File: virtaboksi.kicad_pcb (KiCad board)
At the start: 2 copper layers, 50 x 71.9 mm, 61 parts, among them J1 Panel_01x08, J2 Ext_01x05, J3 Powerpole 01x02, J4 Powerpole 01x02, J5 Powerpole 01x02, J6 Conn_01x03_Male, J7 TagConnect_TC2030-NL, Q1 2N7002, Q2 IRF4905, Q3 IRF4905, Q4 2N7002, Q5 IRF4905, Q6 IRF4905, Q7 2N7002, Q8 IRF4905, Q9 IRF4905, U1 SRV05-4, U2 AMSRI-783.3-NZ, U3 STM8S003F3P, U4 SRV05-4, U5 SP3485EN

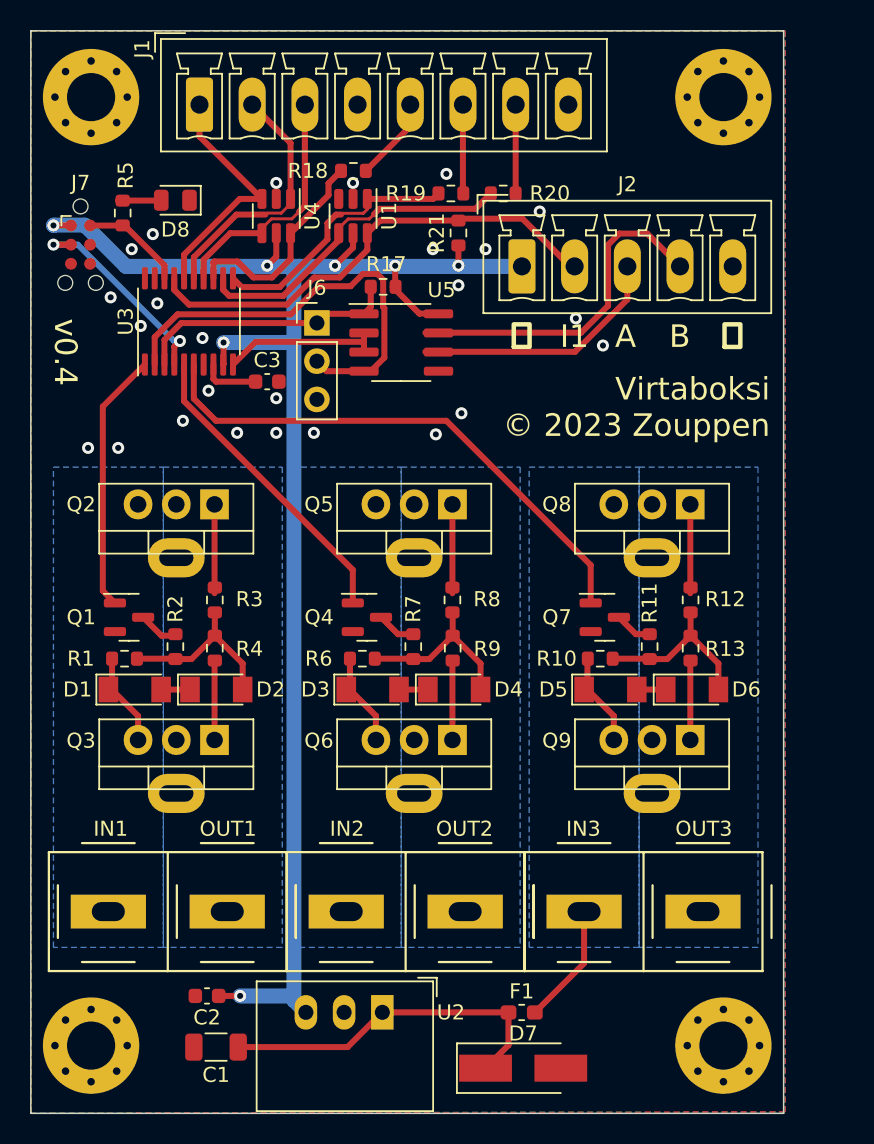
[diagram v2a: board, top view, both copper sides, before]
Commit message: Update solder mask, do final tweaks, make it pass ERC & DRC
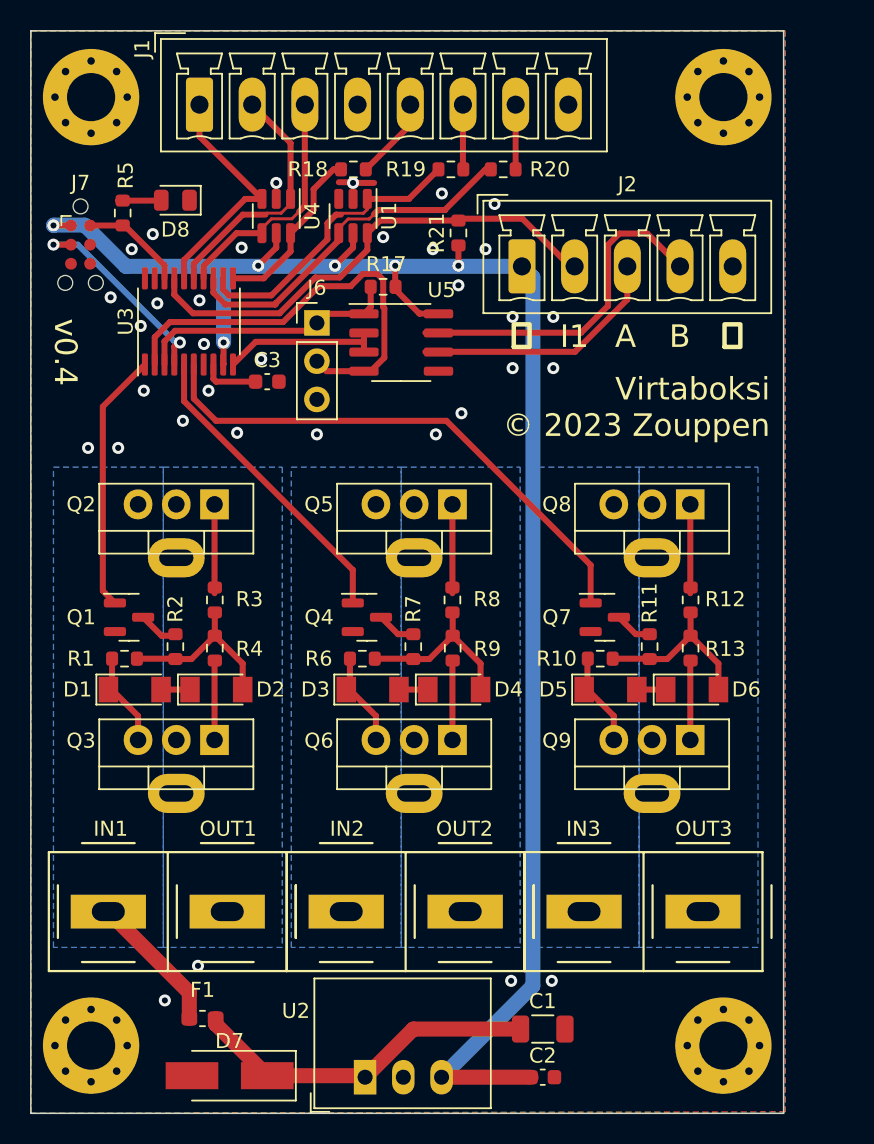
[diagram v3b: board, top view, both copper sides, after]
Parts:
- J6: value Conn_01x03_Male -> Optional_01x03
- moved C2 22.9 mm to (141.5, 109.5), turned to 0 degrees
- moved C1 21.7 mm to (141.5, 106.3), turned to 0 degrees
- moved F1 21.2 mm to (118.9, 105.6), turned to 0 degrees
- moved D7 19.5 mm to (120.7, 109.4), turned to 180 degrees
- moved U2 4.46 mm to (129.7, 109.5), turned to 0 degrees
- moved R19 1.60 mm to (135.4, 49.2)
- moved R20 1.60 mm to (138.9, 49.2)
- moved R18 0.10 mm to (128.9, 49.2)
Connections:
- F1 pad 1: /GROUP3 IN -> /GROUP1 IN
- U3 pad 11: /LED2 -> /LED1
- U3 pad 12: /LED3 -> /LED2
- U3 pad 13: /LED1 -> /LED3
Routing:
- net /GROUP1 IN: track 5.99 -> 15.3 mm
- net +3.3V: track 106.0 -> 114.8 mm, vias 7 -> 6
- net /GROUP3 IN: track 14.0 -> 5.99 mm
- net /LED1: track 14.4 -> 11.7 mm
- net GND: track 0.00 -> 2.36 mm, vias 25 -> 34
- net /LED2: track 17.5 -> 19.7 mm
- net /LED3: track 22.4 -> 24.3 mm
- net Net-(J1-Pad6): track 5.91 -> 4.31 mm
- net Net-(J1-Pad7): track 5.90 -> 4.30 mm
- net /IN1: track 31.3 -> 32.0 mm

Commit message: Reannotate everything
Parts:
- renumbered D7 to D1, D8 to D2, D1 to D3, D2 to D4, D3 to D5, D4 to D6, D5 to D7, D6 to D8, J6 to J1, J1 to J3, J3 to J4, J4 to J5, J5 to J6, R21 to R1, R4 to R10, R6 to R11, R7 to R12, R8 to R13, R9 to R14, R10 to R15, R11 to R16, R12 to R17, R13 to R18, R18 to R2, R19 to R3, R20 to R4, R17 to R5, R5 to R6, R1 to R7, R2 to R8, R3 to R9, U4 to U1, U1 to U3, U5 to U4, U3 to U5

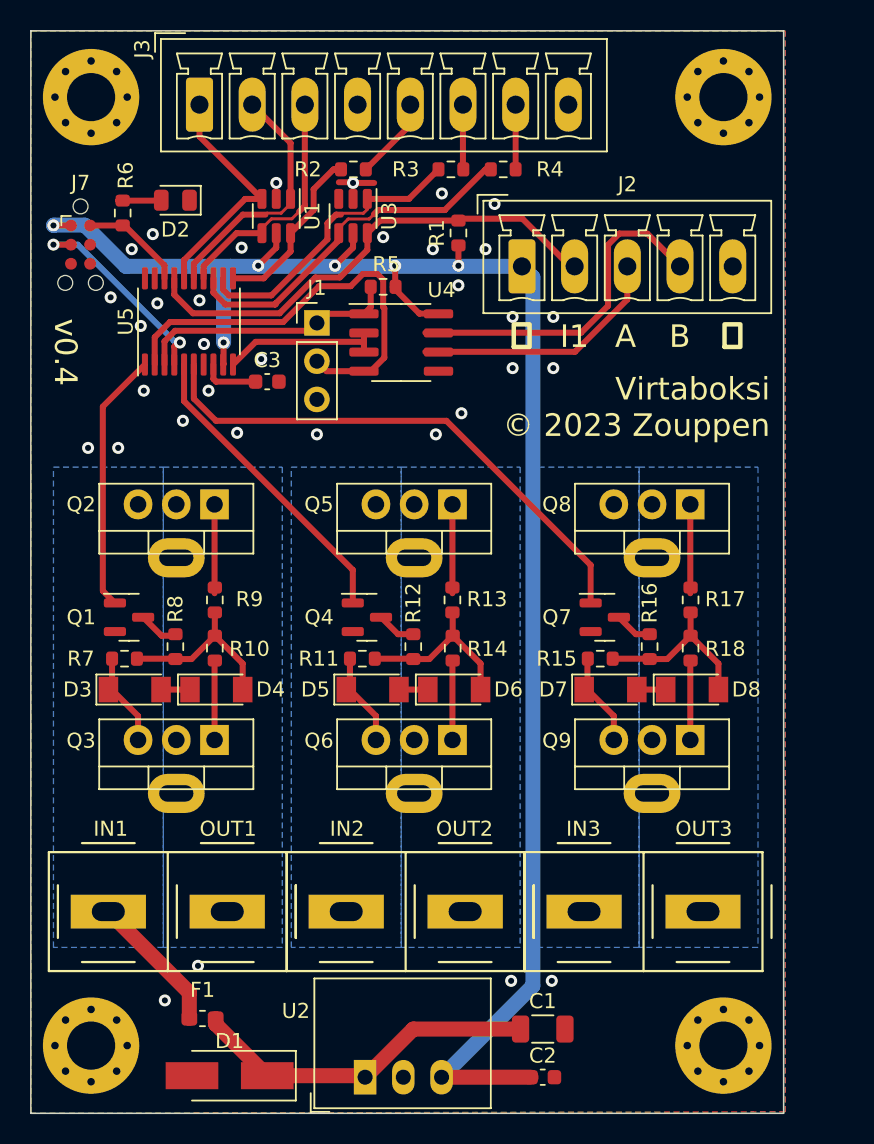
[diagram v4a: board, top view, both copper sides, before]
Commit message: Throw fuse out of the window, clear space left of J2, add 2 extra pins
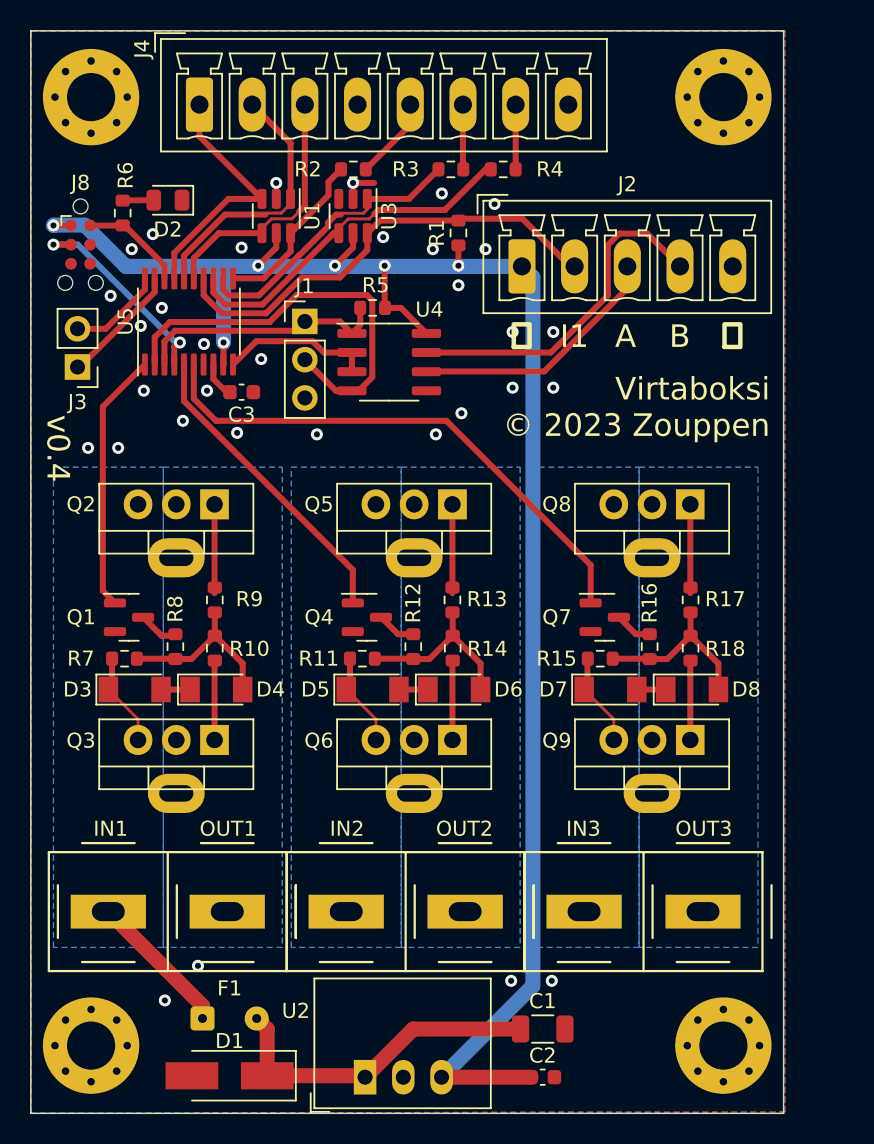
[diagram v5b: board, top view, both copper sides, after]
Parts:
- added J3: Optional_01x02_Male, Connector_PinHeader_2.54mm:PinHeader_1x02_P2.54mm_Vertical, F.Cu at (110.6, 62.3)
- F1: footprint Fuse:Fuse_0603_1608Metric_Pad1.05x0.95mm_HandSolder -> Connector_Wire:SolderWire-0.1sqmm_1x02_P3.6mm_D0.4mm_OD1mm
- moved C3 1.84 mm to (121.5, 64.0)
- moved R5 1.57 mm to (130.2, 58.4)
- moved U4 1.53 mm to (131.3, 62.0)
- moved J1 0.81 mm to (125.7, 59.3)
- moved D2 0.50 mm to (116.6, 51.2)
- renumbered J3 to J4, J4 to J5, J5 to J6, J6 to J7, J7 to J8
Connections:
- U5 pad 14: /IN4 -> /IN1
- U5 pad 15: /IN3 -> /IN4
- U5 pad 16: /IN2 -> /IN3
- U5 pad 17: /IN1 -> /IN2
- U5 pad 19: unconnected-(U5-Pad19) -> /EXTRA1
- U5 pad 20: unconnected-(U5-Pad20) -> /EXTRA2
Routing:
- net /EXTRA1: track 0.00 -> 8.10 mm
- net /EXTRA2: track 0.00 -> 6.30 mm
- net +3.3V: track 114.8 -> 116.7 mm
- net /IN1: track 32.0 -> 30.1 mm
- net Net-(C3-Pad1): track 3.83 -> 2.42 mm
- net Net-(C1-Pad1): track 23.4 -> 22.3 mm
- net GND: track 2.36 -> 1.40 mm, vias 34 -> 33
- net /IN3: track 16.7 -> 17.7 mm
- net /IN4: track 16.1 -> 17.1 mm
- net /IN2: track 16.1 -> 17.0 mm
- net /TX: track 29.2 -> 28.4 mm
- net /RX: track 17.5 -> 16.8 mm
- net Net-(D2-Pad2): track 2.66 -> 2.07 mm

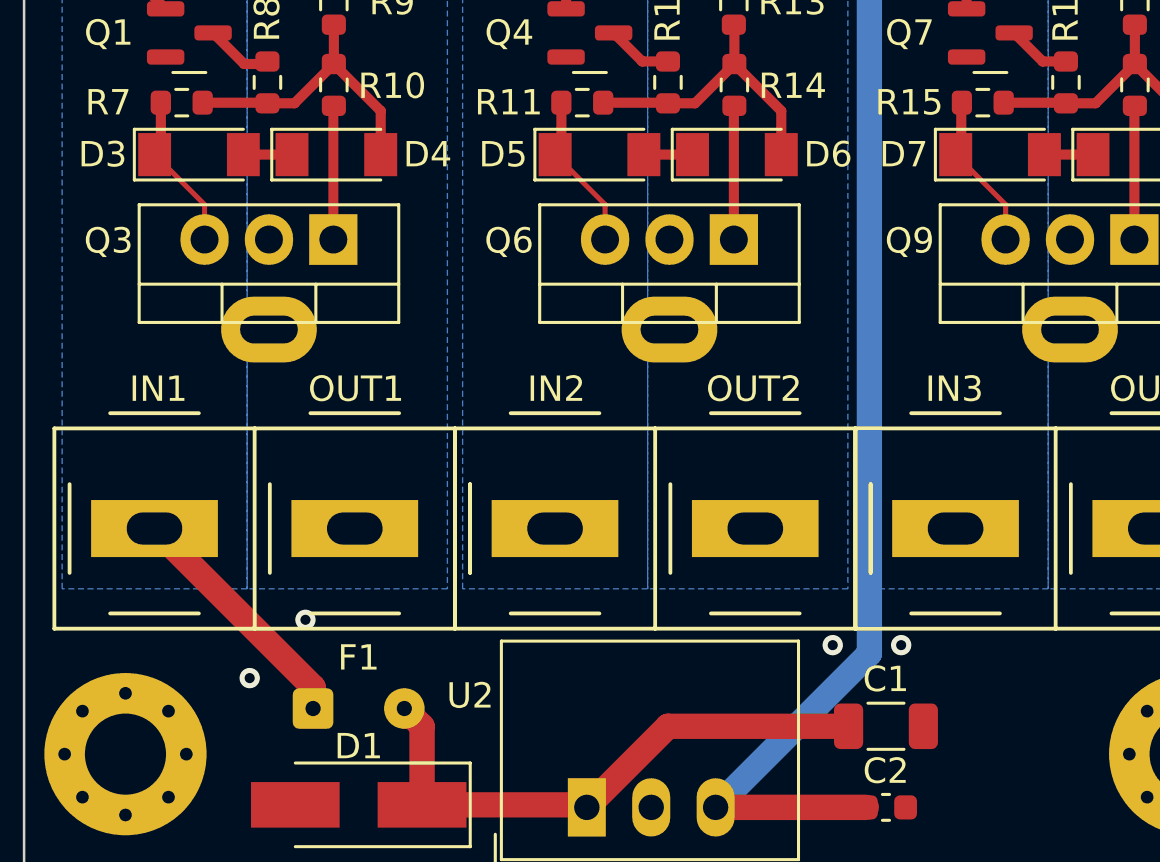
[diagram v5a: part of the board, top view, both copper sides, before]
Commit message: Add makeshift fuse
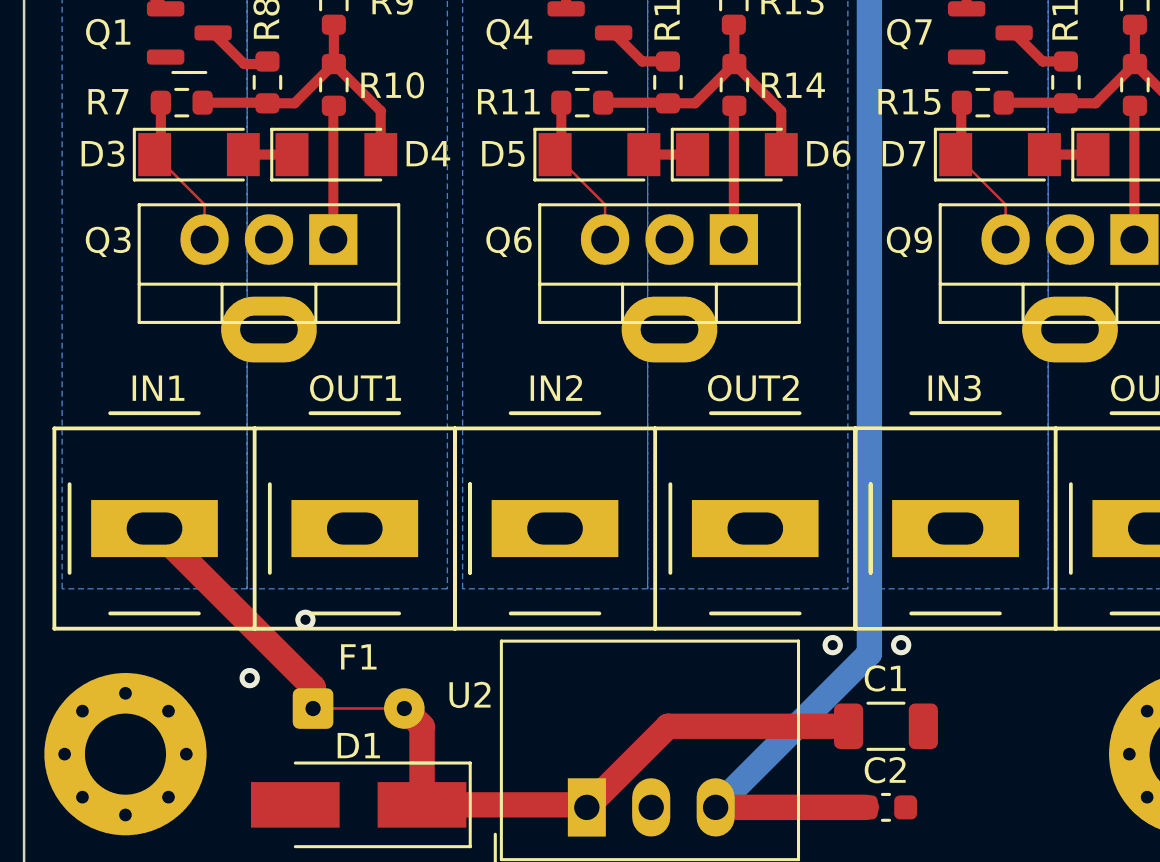
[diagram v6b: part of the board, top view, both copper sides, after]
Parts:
- F1: footprint Connector_Wire:SolderWire-0.1sqmm_1x02_P3.6mm_D0.4mm_OD1mm -> Own parts:Fuse-kindof_1x02_P3.6mm_D0.4mm_OD1mm
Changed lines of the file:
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@@
     )
   )
-  (footprint "Connector_Wire:SolderWire-0.1sqmm_1x02_P3.6mm_D0.4mm_OD1mm" (layer "F.Cu")
+  (footprint "Own parts:Fuse-kindof_1x02_P3.6mm_D0.4mm_OD1mm" (layer "F.Cu")
     (at 118.9 105.6)
     (descr "Soldered wire connection, for 2 times 0.1 mm² wires, basic insulation, conductor diameter 0.4mm, outer diameter 1mm, size source Multi-Contact FLEXI-E 0.1 (https://ec.staubli.com/AcroFiles/Catalogues/TM_Cab-Main-11014119_(en)_hi.pdf), bend radius 3 times outer diameter, generated with kicad-footprint-generator")
@@
       (effects (font (size 0.65 0.65) (thickness 0.1)))
     )
-    (fp_line (start 4.9 1.3) (end 4.9 -1.3) (layer "F.CrtYd") (width 0.05))
+    (fp_rect (start 2.85 -0.05) (end 0.75 0.05) (layer "F.Cu") (width 0) (fill solid))
     (fp_line (start 1.3 -1.3) (end -1.3 -1.3) (layer "F.CrtYd") (width 0.05))
-    (fp_line (start -1.3 -1.3) (end -1.3 1.3) (layer "F.CrtYd") (width 0.05))
+    (fp_line (start 4.9 -1.3) (end 2.3 -1.3) (layer "F.CrtYd") (width 0.05))
     (fp_line (start 2.3 -1.3) (end 2.3 1.3) (layer "F.CrtYd") (width 0.05))
-    (fp_line (start -1.3 1.3) (end 1.3 1.3) (layer "F.CrtYd") (width 0.05))
-    (fp_line (start 2.3 1.3) (end 4.9 1.3) (layer "F.CrtYd") (width 0.05))
     (fp_line (start 1.3 1.3) (end 1.3 -1.3) (layer "F.CrtYd") (width 0.05))
-    (fp_line (start 4.9 -1.3) (end 2.3 -1.3) (layer "F.CrtYd") (width 0.05))
+    (fp_line (start 4.9 1.3) (end 4.9 -1.3) (layer "F.CrtYd") (width 0.05))
+    (fp_line (start 2.3 1.3) (end 4.9 1.3) (layer "F.CrtYd") (width 0.05))
+    (fp_line (start -1.3 1.3) (end 1.3 1.3) (layer "F.CrtYd") (width 0.05))
+    (fp_line (start -1.3 -1.3) (end -1.3 1.3) (layer "F.CrtYd") (width 0.05))
     (fp_circle (center 3.6 0) (end 4.1 0) (layer "F.Fab") (width 0.1) (fill none))
     (fp_circle (center 0 0) (end 0.5 0) (layer "F.Fab") (width 0.1) (fill none))
@@
     (pad "2" thru_hole circle (at 3.6 0) (size 1.6 1.6) (drill 0.6) (layers *.Cu *.Mask)
       (net 5 "Net-(C1-Pad1)") (pintype "passive"))
+    (zone (net 0) (net_name "") (layer "F.Cu") (hatch edge 0.508)
+      (connect_pads (clearance 0))
+      (min_thickness 0.254)
+      (keepout (tracks allowed) (vias allowed) (pads allowed) (copperpour not_allowed) (footprints allowed))
+      (fill (thermal_gap 0.508) (thermal_bridge_width 0.508))
+      (polygon
+        (pts
+          (xy 121.9 106.1)
+          (xy 119.7 106.1)
+          (xy 119.7 105.1)
+          (xy 121.9 105.1)
+        )
+      )
+    )
     (model "${KICAD6_3DMODEL_DIR}/Connector_Wire.3dshapes/SolderWire-0.1sqmm_1x02_P3.6mm_D0.4mm_OD1mm.wrl"
       (offset (xyz 0 0 0))
@@
   (via (at 123.8 50.1) (size 0.8) (drill 0.4) (layers "F.Cu" "B.Cu") (free) (net 1))
   (segment (start 112.895 83.725) (end 112.87 83.75) (width 0.4) (layer "F.Cu") (net 2))
-  (segment (start 114.62 85.72) (end 112.65 83.75) (width 0.2) (layer "F.Cu") (net 2))
   (segment (start 118.9 104.755) (end 112.645 98.5) (width 1) (layer "F.Cu") (net 2))
+  (segment (start 114.62 87.1) (end 114.62 85.72) (width 0.1) (layer "F.Cu") (net 2))
   (segment (start 112.895 81.85) (end 112.895 83.725) (width 0.4) (layer "F.Cu") (net 2))
+  (segment (start 114.62 85.72) (end 112.65 83.75) (width 0.1) (layer "F.Cu") (net 2))
   (segment (start 118.9 105.6) (end 118.9 104.755) (width 1) (layer "F.Cu") (net 2))
-  (segment (start 114.62 87.1) (end 114.62 85.72) (width 0.2) (layer "F.Cu") (net 2))
   (segment (start 128.695 81.85) (end 128.695 83.725) (width 0.4) (layer "F.Cu") (net 3))
-  (segment (start 130.42 87.1) (end 130.42 85.72) (width 0.2) (layer "F.Cu") (net 3))
+  (segment (start 130.42 85.72) (end 128.45 83.75) (width 0.1) (layer "F.Cu") (net 3))
   (segment (start 128.695 83.725) (end 128.67 83.75) (width 0.4) (layer "F.Cu") (net 3))
-  (segment (start 130.42 85.72) (end 128.45 83.75) (width 0.2) (layer "F.Cu") (net 3))
+  (segment (start 130.42 87.1) (end 130.42 85.72) (width 0.1) (layer "F.Cu") (net 3))
+  (segment (start 146.22 85.72) (end 144.25 83.75) (width 0.1) (layer "F.Cu") (net 4))
+  (segment (start 146.22 87.1) (end 146.22 85.72) (width 0.1) (layer "F.Cu") (net 4))
   (segment (start 144.47 81.875) (end 144.495 81.85) (width 0.4) (layer "F.Cu") (net 4))
-  (segment (start 146.22 87.1) (end 146.22 85.72) (width 0.2) (layer "F.Cu") (net 4))
-  (segment (start 146.22 85.72) (end 144.25 83.75) (width 0.2) (layer "F.Cu") (net 4))
   (segment (start 144.47 83.75) (end 144.47 81.875) (width 0.4) (layer "F.Cu") (net 4))
   (segment (start 123.2 109.4) (end 129.6 109.4) (width 1) (layer "F.Cu") (net 5))
